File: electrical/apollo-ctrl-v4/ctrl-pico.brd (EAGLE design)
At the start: 88.6 x 88.9 mm, 43 parts, among them J1 ESP32-PICO-KIT, J2 DNP, J3 DNP, J6 DISPLAY_RIGHT, J7 DISPLAY_LEFT, U1 DNP (24LC01)

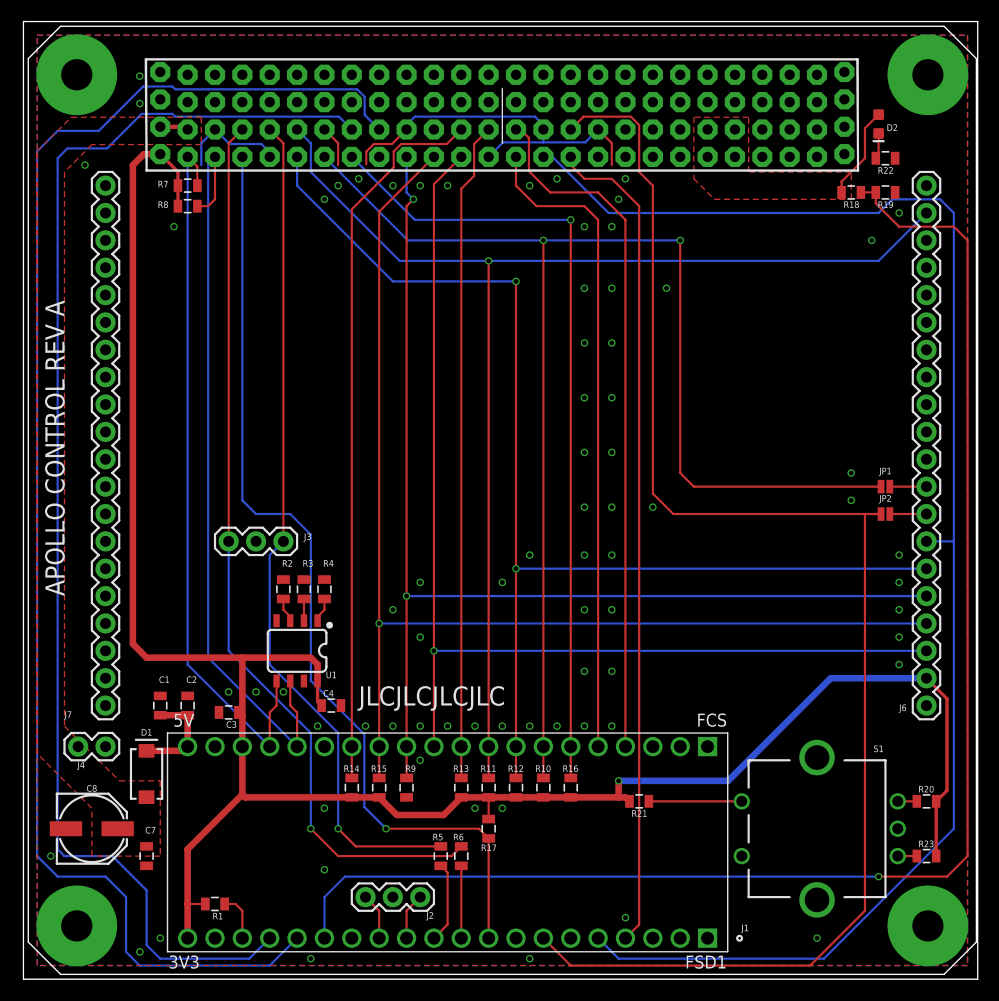
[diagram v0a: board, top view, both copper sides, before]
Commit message: Add buzzer to Apollo control board and move capacitor away from the USB port
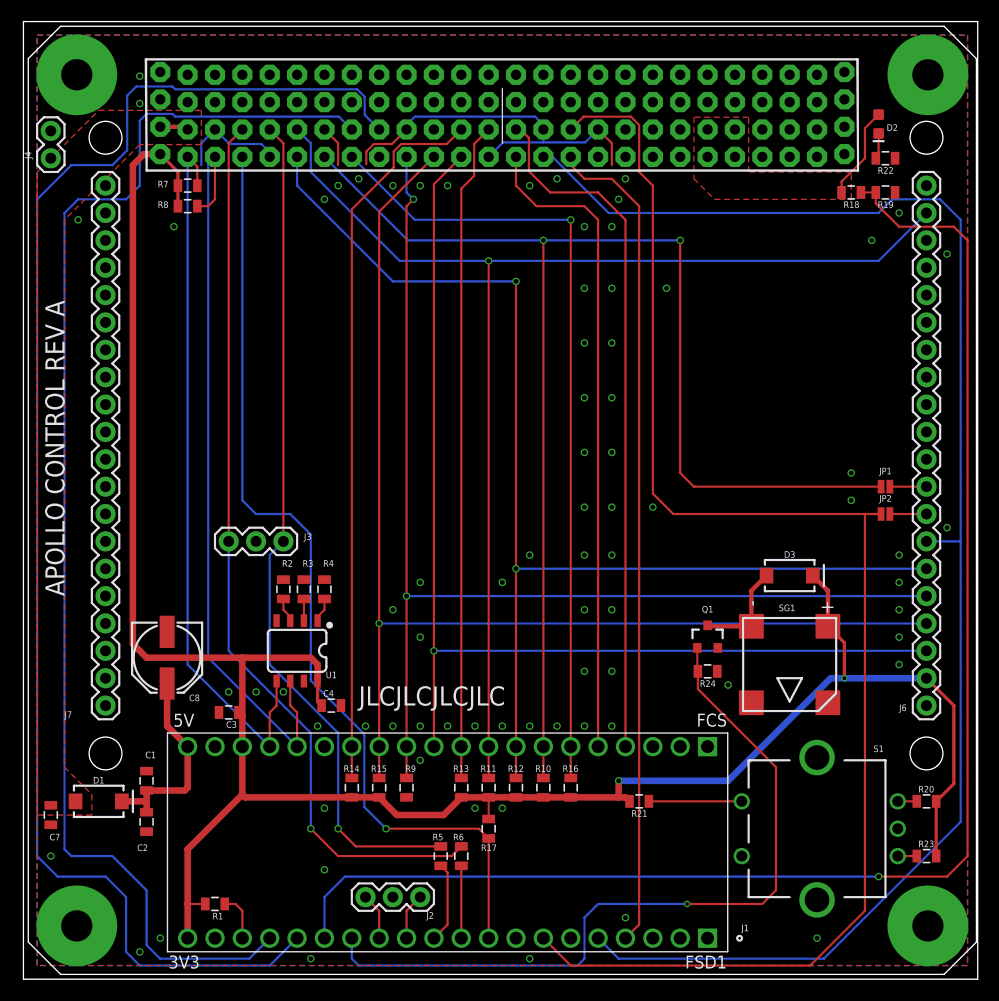
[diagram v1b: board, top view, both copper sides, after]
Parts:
- added D3: 3A, SparkFun-DiscreteSemi:SMA-DIODE
- added Q1: SOT23-3, SparkFun-DiscreteSemi:SOT23-3
- added R24: 10K, apollo-ctrl-v4:0805
- added SG1: BUZZER-POL, apollo-ctrl-v4:BUZZER-SMT-4
- D1: value 497-6577-1-ND -> 3A
- J4: value (none) -> DNP
- moved J4 57.4 mm to (2.54, 78.7), turned to 270 degrees
- moved C8 17.3 mm to (13.3, 29.8), turned to 270 degrees
- moved C2 11.4 mm to (11.4, 14.6), turned to 270 degrees
- moved C7 9.67 mm to (2.54, 15.2)
- moved C1 7.10 mm to (11.4, 18.4)
- moved D1 5.12 mm to (6.99, 16.5), turned to 0 degrees
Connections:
- new net BD: D3.A, Q1.3, SG1.BM
- net +3V3: now also D3.C, SG1.BP
- net +5V: no longer C8.+
- net ADC2: now also Q1.1, R24.2
- net GND: now also Q1.2, R24.1
- net USB5V: now also C8.+
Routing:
- net ADC2: track 0.00 -> 72.2 mm, vias 0 -> 1
- net +3V3: track 196.5 -> 207.7 mm, vias 1 -> 2
- net BD: track 0.00 -> 9.39 mm
- net USB5V: track 9.42 -> 18.7 mm
- net GPIO22: track 139.8 -> 141.0 mm
- net ADC3: track 121.4 -> 120.7 mm
- net GND: vias 74 -> 77
